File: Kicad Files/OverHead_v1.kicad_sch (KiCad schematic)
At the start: 12 parts, among them U1 ATMega2560

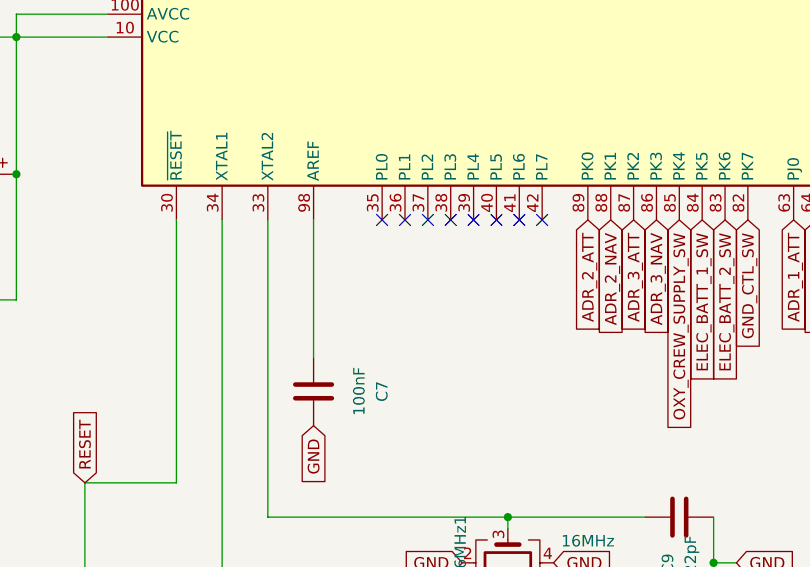
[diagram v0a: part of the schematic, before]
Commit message: Fixed some issues with the code and path on remote drive
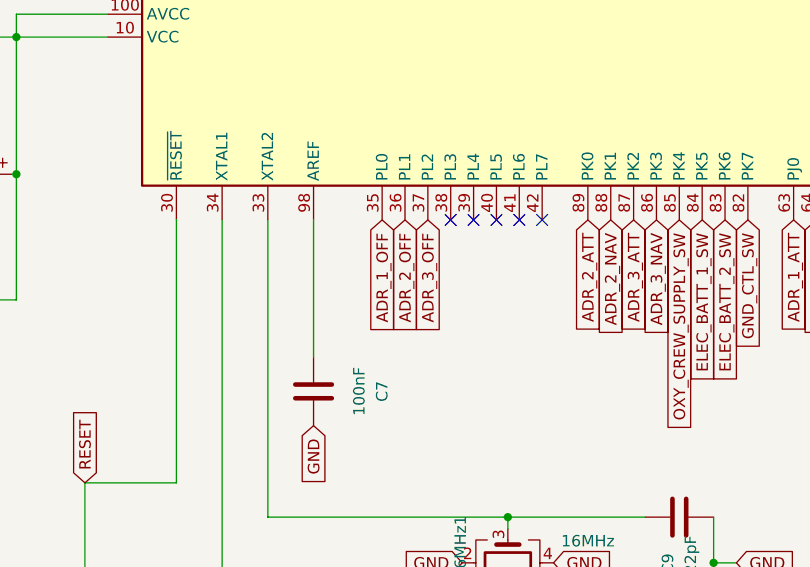
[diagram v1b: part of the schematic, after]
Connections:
- net ADR_1_OFF: now reaches U1.35 (PL0)
- net ADR_2_OFF: now reaches U1.36 (PL1)
- net ADR_3_OFF: now reaches U1.37 (PL2)
- no-connect marks 25 -> 22
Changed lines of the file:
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@@
-	)
-	(no_connect
-		(at 82.55 106.68)
 	)
 	(no_connect
@@
 	)
 	(no_connect
-		(at 85.09 106.68)
-	)
-	(no_connect
 		(at 138.43 66.04)
 	)
 	(no_connect
 		(at 146.05 106.68)
-	)
-	(no_connect
-		(at 87.63 106.68)
 	)
 	(no_connect
@@
 		)
 	)
+	(global_label "ADR_3_OFF"
+		(shape input)
+		(at 87.63 106.68 270)
+		(fields_autoplaced yes)
+		(effects
+			(font
+				(size 1.27 1.27)
+			)
+			(justify right)
+		)
+		(property "Intersheetrefs" "${INTERSHEET_REFS}"
+			(at 87.63 119.9462 90)
+			(effects
+				(font
+					(size 1.27 1.27)
+				)
+				(justify right)
+				(hide yes)
+			)
+		)
+	)
 	(global_label "BEACON_ON"
 		(shape input)
@@
 		)
 	)
+	(global_label "ADR_2_OFF"
+		(shape input)
+		(at 85.09 106.68 270)
+		(fields_autoplaced yes)
+		(effects
+			(font
+				(size 1.27 1.27)
+			)
+			(justify right)
+		)
+		(property "Intersheetrefs" "${INTERSHEET_REFS}"
+			(at 85.09 119.9462 90)
+			(effects
+				(font
+					(size 1.27 1.27)
+				)
+				(justify right)
+				(hide yes)
+			)
+		)
+	)
 	(global_label "CLK1"
 		(shape input)
@@
 				(hide yes)
 			)
+		)
+	)
+	(global_label "ADR_1_OFF"
+		(shape input)
+		(at 82.55 106.68 270)
+		(fields_autoplaced yes)
+		(effects
+			(font
+				(size 1.27 1.27)
+			)
+			(justify right)
+		)
+		(property "Intersheetrefs" "${INTERSHEET_REFS}"
+			(at 82.55 119.9462 90)
+			(effects
+				(font
+					(size 1.27 1.27)
+				)
+				(justify right)
+				(hide yes)
+			)

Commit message: Improved pcb design by adding a dip-switch to alter I2C physical address and other small design improvements
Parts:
- XT16MHz1: footprint Crystal:Crystal_SMD_EuroQuartz_MJ-4Pin_5.0x3.2mm_HandSoldering -> Crystal:Crystal_SMD_EuroQuartz_MQ-4Pin_7.0x5.0mm_HandSoldering
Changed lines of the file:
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@@
 			)
 		)
-		(property "Footprint" "Crystal:Crystal_SMD_EuroQuartz_MJ-4Pin_5.0x3.2mm_HandSoldering"
+		(property "Footprint" "Crystal:Crystal_SMD_EuroQuartz_MQ-4Pin_7.0x5.0mm_HandSoldering"
 			(at 96.52 144.78 0)
 			(effects

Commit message: New STL files for APU OVHD element, other coming in the next few weeks
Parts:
- U1: footprint SFLibrary:TQFP100-0.5-14X14MM -> PCM_SFLibrary:TQFP100-0.5-14X14MM
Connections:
- net SCL: now also U1.43 (PD0); no longer U1.44 (PD1)
- net SDA: now also U1.44 (PD1); no longer U1.43 (PD0)
- net L_XFER_SW renamed CTR_TK_PUMP_1_SW
- net NOSMOKING_OFF renamed NOSMOKING_SIGN
- net NOSMOKING_ON: no longer names the net of U1.50 (PD7)
- net R_XFER_SW renamed CTR_TK_PUMP_2_SW
- net SEATBELTS_OFF: no longer names the net of U1.46 (PD3)
- net SEATBELTS_ON renamed SEATBELTS_SIGN
- no-connect marks 22 -> 24
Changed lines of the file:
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@@
 (kicad_sch
-	(version 20231120)
+	(version 20250114)
 	(generator "eeschema")
-	(generator_version "8.0")
+	(generator_version "9.0")
 	(paper "A4")
+	(text "DM13A Drivers"
+		(exclude_from_sim no)
+		(at 65.532 56.134 0)
+		(effects
+			(font
+				(size 1.27 1.27)
+			)
+		)
+	)
 	(junction
 		(at 33.02 76.2)
@@
 	)
 	(no_connect
+		(at 146.05 66.04)
+	)
+	(no_connect
 		(at 140.97 106.68)
 	)
 	(no_connect
+		(at 135.89 66.04)
+	)
+	(no_connect
 		(at 138.43 106.68)
 	)
@@
 		)
 	)
-	(text "DM13A Drivers"
-		(exclude_from_sim no)
-		(at 65.532 56.134 0)
-		(effects
-			(font
-				(size 1.27 1.27)
-			)
-		)
-	)
 	(global_label "ANTI_ICE_ENG2_SW"
 		(shape input)
@@
 		)
 	)
-	(global_label "SCL"
-		(shape output)
-		(at 130.81 57.15 90)
-		(fields_autoplaced yes)
-		(effects
-			(font
-				(size 1.27 1.27)
-			)
-			(justify left)
-		)
-		(property "Intersheetrefs" "${INTERSHEET_REFS}"
-			(at 130.81 50.6572 90)
-			(effects
-				(font
-					(size 1.27 1.27)
-				)
-				(justify left)
-				(hide yes)
-			)
-		)
-	)
 	(global_label "ANTI_ICE_ENG1_SW"
 		(shape input)
@@
 		)
 	)
-	(global_label "L_XFER_SW"
+	(global_label "CTR_TK_PUMP_1_SW"
 		(shape input)
 		(at 163.83 106.68 270)
@@
 		)
 		(property "Intersheetrefs" "${INTERSHEET_REFS}"
-			(at 163.83 120.0065 90)
+			(at 163.83 128.4731 90)
 			(effects
 				(font
@@
 		)
 	)
+	(global_label "NOSMOKING_SIGN"
+		(shape input)
+		(at 158.75 66.04 90)
+		(fields_autoplaced yes)
+		(effects
+			(font
+				(size 1.27 1.27)
+			)
+			(justify left)
+		)
+		(property "Intersheetrefs" "${INTERSHEET_REFS}"
+			(at 158.75 46.5447 90)
+			(effects
+				(font
+					(size 1.27 1.27)
+				)
+				(justify left)
+				(hide yes)
+			)
+		)
+	)
 	(global_label "LCH2"
 		(shape input)
@@
 		)
 	)
-	(global_label "NOSMOKING_OFF"
-		(shape input)
-		(at 158.75 66.04 90)
+	(global_label "SCL"
+		(shape output)
+		(at 128.27 57.15 90)
 		(fields_autoplaced yes)
 		(effects
@@
 		)
 		(property "Intersheetrefs" "${INTERSHEET_REFS}"
-			(at 158.75 47.4518 90)
+			(at 128.27 50.6572 90)
 			(effects
 				(font
@@
 		)
 	)
+	(global_label "SDA"
+		(shape output)
+		(at 130.81 57.15 90)
+		(fields_autoplaced yes)
+		(effects
+			(font
+				(size 1.27 1.27)
+			)
+			(justify left)
+		)
+		(property "Intersheetrefs" "${INTERSHEET_REFS}"
+			(at 130.81 50.5967 90)
+			(effects
+				(font
+					(size 1.27 1.27)
+				)
+				(justify left)
+				(hide yes)
+			)
+		)
+	)
 	(global_label "GPWS_SYS_SW"
 		(shape input)
@@
 		)
 	)
-	(global_label "NOSMOKING_ON"
-		(shape input)
-		(at 146.05 66.04 90)
-		(fields_autoplaced yes)
-		(effects
-			(font
-				(size 1.27 1.27)
-			)
-			(justify left)
-		)
-		(property "Intersheetrefs" "${INTERSHEET_REFS}"
-			(at 146.05 48.2985 90)
-			(effects
-				(font
-					(size 1.27 1.27)
-				)
-				(justify left)
-				(hide yes)
-			)
-		)
-	)
 	(global_label "STROBE_ON"
 		(shape input)
@@
 		)
 	)
-	(global_label "SDA"
-		(shape output)
-		(at 128.27 57.15 90)
-		(fields_autoplaced yes)
-		(effects
-			(font
-				(size 1.27 1.27)
-			)
-			(justify left)
-		)
-		(property "Intersheetrefs" "${INTERSHEET_REFS}"
-			(at 128.27 50.5967 90)
-			(effects
-				(font
-					(size 1.27 1.27)
-				)
-				(justify left)
-				(hide yes)
-			)
-		)
-	)
 	(global_label "ADR_1_NAV"
 		(shape input)
@@
 		)
 	)
-	(global_label "SEATBELTS_ON"
+	(global_label "SEATBELTS_SIGN"
 		(shape input)
 		(at 133.35 66.04 90)
@@
 		)
 		(property "Intersheetrefs" "${INTERSHEET_REFS}"
-			(at 133.35 49.3873 90)
-			(effects
-				(font
-					(size 1.27 1.27)
-				)
-				(justify left)
-				(hide yes)
-			)
-		)
-	)
-	(global_label "SEATBELTS_OFF"
-		(shape input)
-		(at 135.89 66.04 90)
-		(fields_autoplaced yes)
-		(effects
-			(font
-				(size 1.27 1.27)
-			)
-			(justify left)
-		)
-		(property "Intersheetrefs" "${INTERSHEET_REFS}"
-			(at 135.89 48.5406 90)
+			(at 133.35 47.6335 90)
 			(effects
 				(font
@@
 		)
 	)
-	(global_label "R_XFER_SW"
+	(global_label "CTR_TK_PUMP_2_SW"
 		(shape input)
 		(at 166.37 106.68 270)
@@
 		)
 		(property "Intersheetrefs" "${INTERSHEET_REFS}"
-			(at 166.37 120.2484 90)
+			(at 166.37 128.4731 90)
 			(effects
 				(font
@@
 			)
 		)
-		(property "Footprint" "SFLibrary:TQFP100-0.5-14X14MM"
+		(property "Footprint" "PCM_SFLibrary:TQFP100-0.5-14X14MM"
 			(at 125.73 86.36 0)
 			(effects
@@
 		(at 0 215.9)
 		(size 297.18 187.96)
+		(exclude_from_sim no)
+		(in_bom yes)
+		(on_board yes)
+		(dnp no)
 		(fields_autoplaced yes)
 		(stroke
@@
 		(at 838.2 0)
 		(size 255.27 209.55)
+		(exclude_from_sim no)
+		(in_bom yes)
+		(on_board yes)
+		(dnp no)
 		(fields_autoplaced yes)
 		(stroke
@@
 		(at 0 412.75)
 		(size 298.45 176.53)
+		(exclude_from_sim no)
+		(in_bom yes)
+		(on_board yes)
+		(dnp no)
 		(fields_autoplaced yes)
 		(stroke
@@
 		(at 572.77 412.75)
 		(size 256.54 176.53)
+		(exclude_from_sim no)
+		(in_bom yes)
+		(on_board yes)
+		(dnp no)
 		(fields_autoplaced yes)
 		(stroke
@@
 		(at 571.5 215.9)
 		(size 257.81 187.96)
+		(exclude_from_sim no)
+		(in_bom yes)
+		(on_board yes)
+		(dnp no)
 		(fields_autoplaced yes)
 		(stroke
@@
 		(at 836.93 412.75)
 		(size 257.81 176.53)
+		(exclude_from_sim no)
+		(in_bom yes)
+		(on_board yes)
+		(dnp no)
 		(fields_autoplaced yes)
 		(stroke
@@
 		(at 304.8 412.75)
 		(size 262.89 176.53)
+		(exclude_from_sim no)
+		(in_bom yes)
+		(on_board yes)
+		(dnp no)
 		(fields_autoplaced yes)
 		(stroke
@@
 		(at 1103.63 0)
 		(size 236.22 208.28)
+		(exclude_from_sim no)
+		(in_bom yes)
+		(on_board yes)
+		(dnp no)
 		(fields_autoplaced yes)
 		(stroke
@@
 		(at 1103.63 215.9)
 		(size 236.22 187.96)
+		(exclude_from_sim no)
+		(in_bom yes)
+		(on_board yes)
+		(dnp no)
 		(fields_autoplaced yes)
 		(stroke
@@
 		(at 304.8 0)
 		(size 262.89 209.55)
+		(exclude_from_sim no)
+		(in_bom yes)
+		(on_board yes)
+		(dnp no)
 		(fields_autoplaced yes)
 		(stroke
@@
 		(at 0 596.9)
 		(size 297.18 168.91)
+		(exclude_from_sim no)
+		(in_bom yes)
+		(on_board yes)
+		(dnp no)
 		(fields_autoplaced yes)
 		(stroke
@@
 		(at 838.2 215.9)
 		(size 255.27 187.96)
+		(exclude_from_sim no)
+		(in_bom yes)
+		(on_board yes)
+		(dnp no)
 		(fields_autoplaced yes)
 		(stroke
@@
 		(at 304.8 215.9)
 		(size 262.89 187.96)
+		(exclude_from_sim no)
+		(in_bom yes)
+		(on_board yes)
+		(dnp no)
 		(fields_autoplaced yes)
 		(stroke
@@
 		(at 571.5 0)
 		(size 257.81 209.55)
+		(exclude_from_sim no)
+		(in_bom yes)
+		(on_board yes)
+		(dnp no)
 		(fields_autoplaced yes)
 		(stroke
@@
 		)
 	)
+	(embedded_fonts no)
 )
